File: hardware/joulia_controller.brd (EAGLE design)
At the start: 121 x 68 mm, 42 parts, among them IC1 LM2902D, IC2 LM2902D, U1 MMBT2222ALT1G, U2 MMBT2222ALT1G

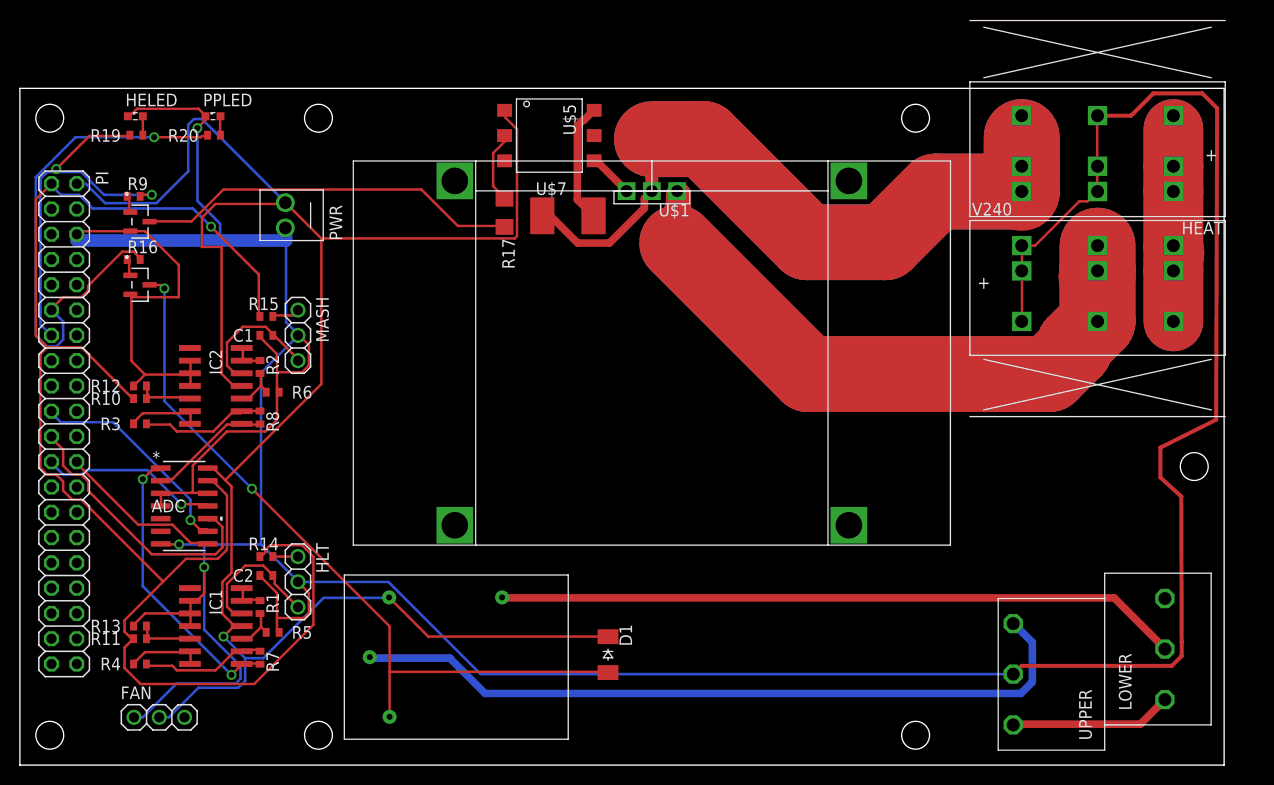
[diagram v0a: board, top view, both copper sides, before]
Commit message: Switches two plugs for one board terminal for 240V connections.
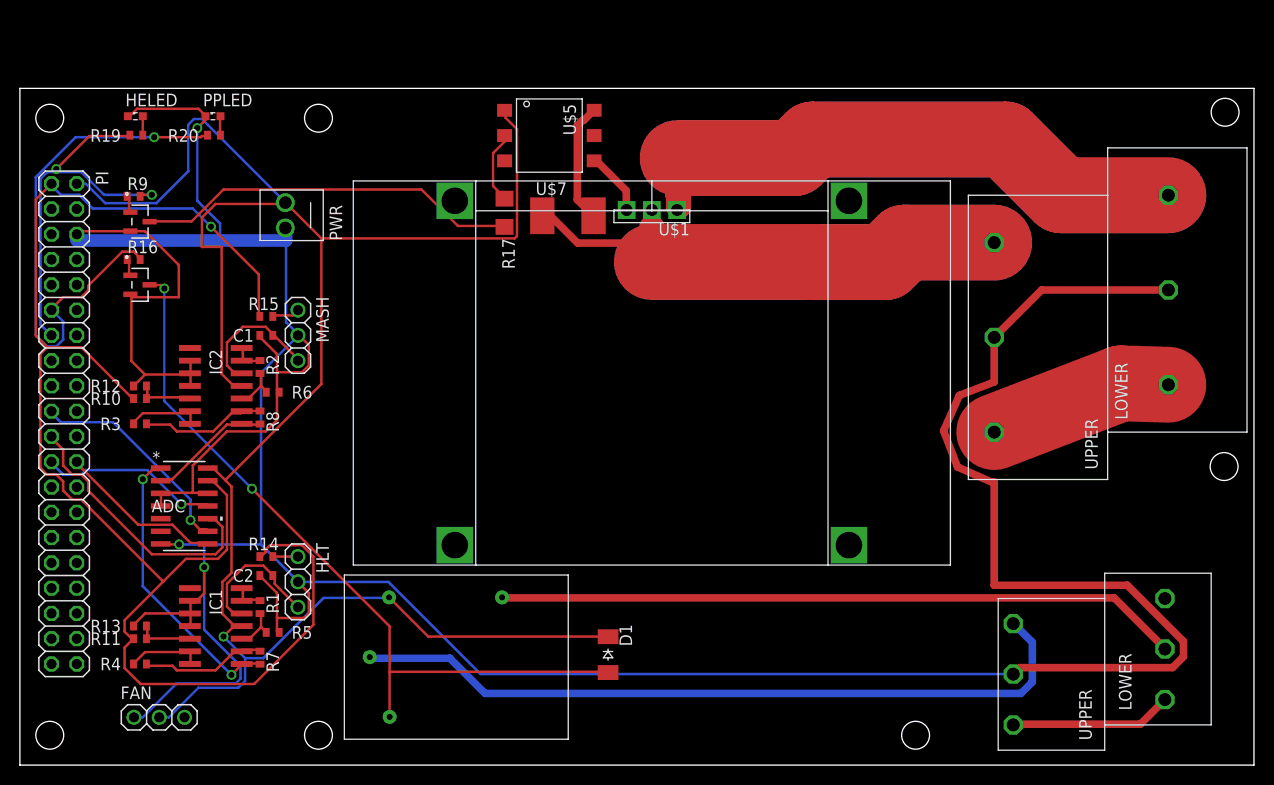
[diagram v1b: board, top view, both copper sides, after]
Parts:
- removed HEAT, V240: PC1720589, digikey:PC-PCV5/3-G-7.62
- added U$6: PC1719028, digikey:PC-MKKDS5/3-9.5
- moved U$2 2.00 mm to (33.5, 58.7)
- moved U$1 1.90 mm to (63.5, 55.8)
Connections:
- net +120: now also U$6.P$1, U$6.P$4; no longer HEAT.P$7, HEAT.P$8, HEAT.P$9, V240.P$4, V240.P$5, V240.P$6
- net -120: now also U$6.P$3; no longer V240.P$1, V240.P$2, V240.P$3
- net GND: now also U$6.P$2, U$6.P$5; no longer HEAT.P$1, HEAT.P$2, HEAT.P$3, V240.P$7, V240.P$8, V240.P$9
- net N$22: now also U$6.P$6; no longer HEAT.P$4, HEAT.P$5, HEAT.P$6
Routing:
- net N$22: track 128.6 -> 95.5 mm
- net +120: track 43.8 -> 18.4 mm
- net GND: track 413.7 -> 388.4 mm
- net -120: track 127.2 -> 116.3 mm
- net N$19: track 4.52 -> 6.41 mm
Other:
- board size 121 x 68 mm -> 124 x 68 mm

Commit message: Move ground to 120V connection.
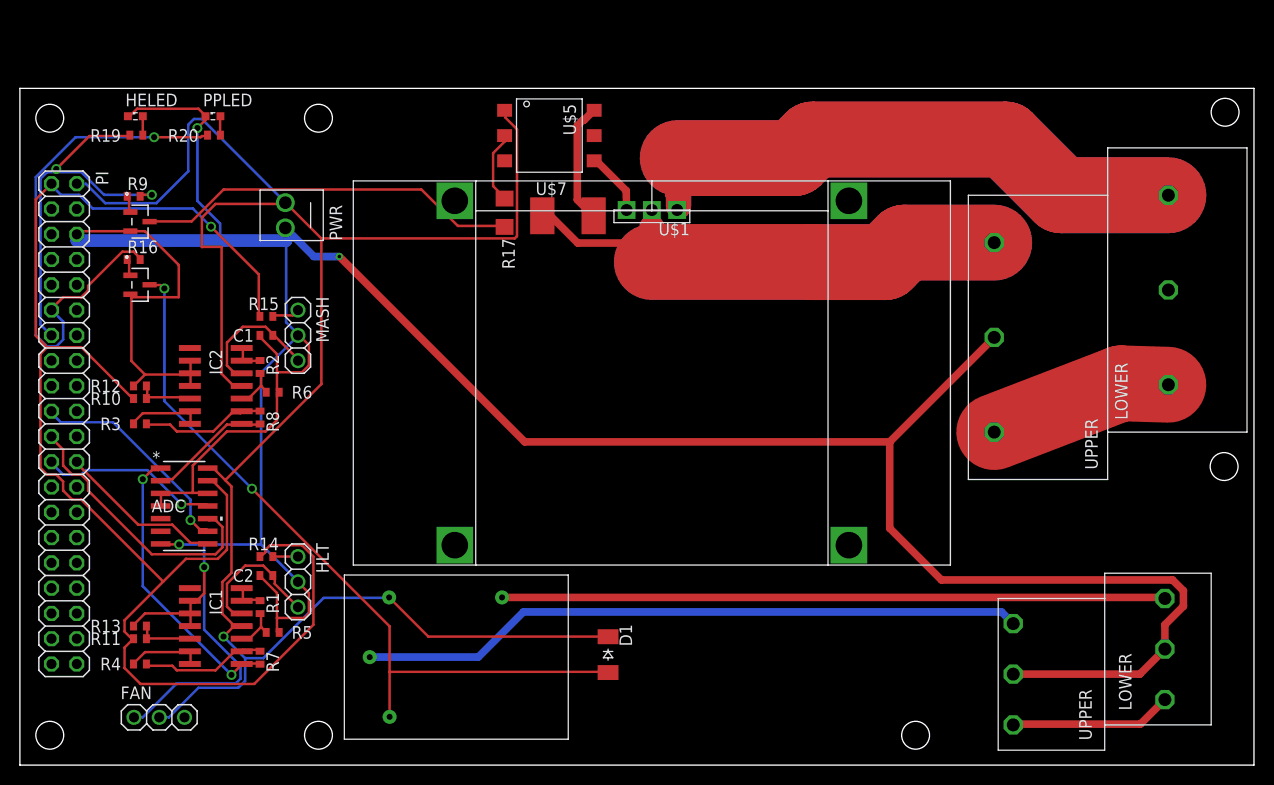
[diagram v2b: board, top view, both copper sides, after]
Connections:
- net 120H: now also U$4.P$3; no longer U$4.P$2
- net GND: now also U$4.P$2; no longer U$6.P$2
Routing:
- net GND: track 388.4 -> 370.3 mm, vias 3 -> 4
- net N$24: track 75.3 -> 67.0 mm
- net 120H: track 68.8 -> 66.6 mm
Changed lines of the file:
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@@
 <wire x1="26.7462" y1="52.705" x2="26.7462" y2="53.8734" width="0.254" layer="16"/>
 <wire x1="27.8892" y1="43.3578" x2="26.7462" y2="44.5008" width="0.254" layer="16"/>
-<wire x1="26.7462" y1="53.8734" x2="26.67" y2="53.975" width="0.254" layer="16"/>
+<wire x1="26.67" y1="53.975" x2="26.7462" y2="53.8734" width="0.254" layer="16"/>
 <wire x1="27.8892" y1="43.3578" x2="27.94" y2="43.18" width="0.254" layer="16"/>
 <wire x1="28.3464" y1="39.4716" x2="25.8318" y2="39.4716" width="0.254" layer="1"/>
@@
 <wire x1="11.5443" y1="4.8006" x2="11.46" y2="4.8" width="0.254" layer="16"/>
 <contactref element="U$4" pad="P$5"/>
-<wire x1="46.2915" y1="9.144" x2="99.7839" y2="9.144" width="0.254" layer="16"/>
-<wire x1="37.0332" y1="18.4023" x2="46.2915" y2="9.144" width="0.254" layer="16"/>
-<wire x1="28.0035" y1="18.4023" x2="37.0332" y2="18.4023" width="0.254" layer="16"/>
-<wire x1="99.7839" y1="9.144" x2="99.81" y2="9.14" width="0.254" layer="16"/>
-<wire x1="28.0035" y1="18.4023" x2="27.94" y2="18.415" width="0.254" layer="16"/>
 <contactref element="U$6" pad="P$5"/>
-<contactref element="U$6" pad="P$2"/>
-<wire x1="115.4" y1="47.74" x2="102.66" y2="47.74" width="0.762" layer="1"/>
-<wire x1="102.66" y1="47.74" x2="97.9" y2="42.98" width="0.762" layer="1"/>
-<wire x1="97.9" y1="42.98" x2="97.9" y2="38.494578125" width="0.762" layer="1"/>
-<wire x1="97.9" y1="38.494578125" x2="94.3965" y2="37.147078125" width="0.762" layer="1"/>
-<wire x1="94.3965" y1="37.147078125" x2="92.815496875" y2="33.589815625" width="0.762" layer="1"/>
-<wire x1="92.815496875" y1="33.589815625" x2="94.212925" y2="29.9565" width="0.762" layer="1"/>
-<wire x1="94.212925" y1="29.9565" x2="97.7701875" y2="28.375496875" width="0.762" layer="1"/>
-<wire x1="97.7701875" y1="28.375496875" x2="97.9" y2="28.425425" width="0.762" layer="1"/>
-<wire x1="97.9" y1="28.425425" x2="97.9" y2="18.0721" width="0.762" layer="1"/>
-<wire x1="116.914" y1="12.4321" x2="116.914" y2="10.8879" width="0.762" layer="1"/>
-<wire x1="116.914" y1="10.8879" x2="115.8221" y2="9.796" width="0.762" layer="1"/>
-<wire x1="97.9" y1="18.0721" x2="111.274" y2="18.0721" width="0.762" layer="1"/>
-<wire x1="111.274" y1="18.0721" x2="116.914" y2="12.4321" width="0.762" layer="1"/>
-<wire x1="100.466" y1="9.796" x2="99.81" y2="9.14" width="0.762" layer="1"/>
-<wire x1="115.8221" y1="9.796" x2="100.466" y2="9.796" width="0.762" layer="1"/>
+<contactref element="U$4" pad="P$2"/>
+<wire x1="99.81" y1="9.14" x2="112.53" y2="9.14" width="0.762" layer="1"/>
+<wire x1="112.53" y1="9.14" x2="115.05" y2="11.66" width="0.762" layer="1"/>
+<wire x1="116.914" y1="15.9679" x2="116.914" y2="17.5121" width="0.762" layer="1"/>
+<wire x1="116.914" y1="17.5121" x2="115.8221" y2="18.604" width="0.762" layer="1"/>
+<wire x1="92.596" y1="18.604" x2="87.4" y2="23.8" width="0.762" layer="1"/>
+<wire x1="115.8221" y1="18.604" x2="92.596" y2="18.604" width="0.762" layer="1"/>
+<wire x1="115.05" y1="11.66" x2="115.05" y2="14.1039" width="0.762" layer="1"/>
+<wire x1="115.05" y1="14.1039" x2="116.914" y2="15.9679" width="0.762" layer="1"/>
+<wire x1="87.4" y1="23.8" x2="87.4" y2="32.48" width="0.762" layer="1"/>
+<wire x1="87.4" y1="32.48" x2="97.9" y2="42.98" width="0.762" layer="1"/>
+<wire x1="87.4" y1="32.48" x2="50.72" y2="32.48" width="0.762" layer="1"/>
+<wire x1="50.72" y1="32.48" x2="32.1" y2="51.1" width="0.762" layer="1"/>
+<via x="32.1" y="51.1" extent="1-16" drill="0.35"/>
+<wire x1="32.1" y1="51.1" x2="29.545" y2="51.1" width="0.762" layer="16"/>
+<wire x1="29.545" y1="51.1" x2="26.67" y2="53.975" width="0.762" layer="16"/>
 </signal>
 <signal name="N$4">
@@
 <contactref element="U$3" pad="P$3"/>
 <contactref element="U$4" pad="P$6"/>
-<wire x1="43.2054" y1="10.7442" x2="35.2044" y2="10.7442" width="0.762" layer="16"/>
-<wire x1="46.7487" y1="7.2009" x2="43.2054" y2="10.7442" width="0.762" layer="16"/>
-<wire x1="100.584" y1="7.2009" x2="46.7487" y2="7.2009" width="0.762" layer="16"/>
-<wire x1="101.727" y1="8.3439" x2="100.584" y2="7.2009" width="0.762" layer="16"/>
-<wire x1="101.727" y1="12.3444" x2="101.727" y2="8.3439" width="0.762" layer="16"/>
-<wire x1="99.8982" y1="14.1732" x2="101.727" y2="12.3444" width="0.762" layer="16"/>
-<wire x1="35.2044" y1="10.7442" x2="35.15" y2="10.85" width="0.762" layer="16"/>
-<wire x1="99.8982" y1="14.1732" x2="99.81" y2="14.22" width="0.762" layer="16"/>
+<wire x1="35.15" y1="10.85" x2="46.05" y2="10.85" width="0.762" layer="16"/>
+<wire x1="46.05" y1="10.85" x2="50.6" y2="15.4" width="0.762" layer="16"/>
+<wire x1="50.6" y1="15.4" x2="98.63" y2="15.4" width="0.762" layer="16"/>
+<wire x1="98.63" y1="15.4" x2="99.81" y2="14.22" width="0.762" layer="16"/>
 </signal>
 <signal name="120H" class="1">
 <contactref element="U$3" pad="P$1"/>
-<contactref element="U$4" pad="P$2"/>
-<wire x1="109.9566" y1="16.8021" x2="48.4632" y2="16.8021" width="0.762" layer="1"/>
-<wire x1="114.9858" y1="11.7729" x2="109.9566" y2="16.8021" width="0.762" layer="1"/>
-<wire x1="48.4632" y1="16.8021" x2="48.45" y2="16.85" width="0.762" layer="1"/>
-<wire x1="114.9858" y1="11.7729" x2="115.05" y2="11.66" width="0.762" layer="1"/>
+<contactref element="U$4" pad="P$3"/>
+<wire x1="48.45" y1="16.85" x2="114.94" y2="16.85" width="0.762" layer="1"/>
+<wire x1="114.94" y1="16.85" x2="115.05" y2="16.74" width="0.762" layer="1"/>
 </signal>
 <signal name="N$28">

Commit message: Better relay layout.
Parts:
- moved U$3 69.7 mm to (100.6, 17.9), turned to 270 degrees
- moved D1 16.0 mm to (74.9, 13.9), turned to 90 degrees
- moved U$4 3.90 mm to (123.6, 1.50)
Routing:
- net N$24: track 67.0 -> 9.49 mm
- net N$18: track 76.1 -> 124.4 mm
- net +5V: track 204.4 -> 243.9 mm
- net 120H: track 66.6 -> 42.0 mm
- net GND: track 370.3 -> 375.6 mm
